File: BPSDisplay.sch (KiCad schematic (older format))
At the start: 22 parts, among them J1 SWD, J2 Conn_02x06_Counter_Clockwise, P1 Conn_02x20_Odd_Even, SW1 Reset, U1 STM32F413RHTx, Y1 8M

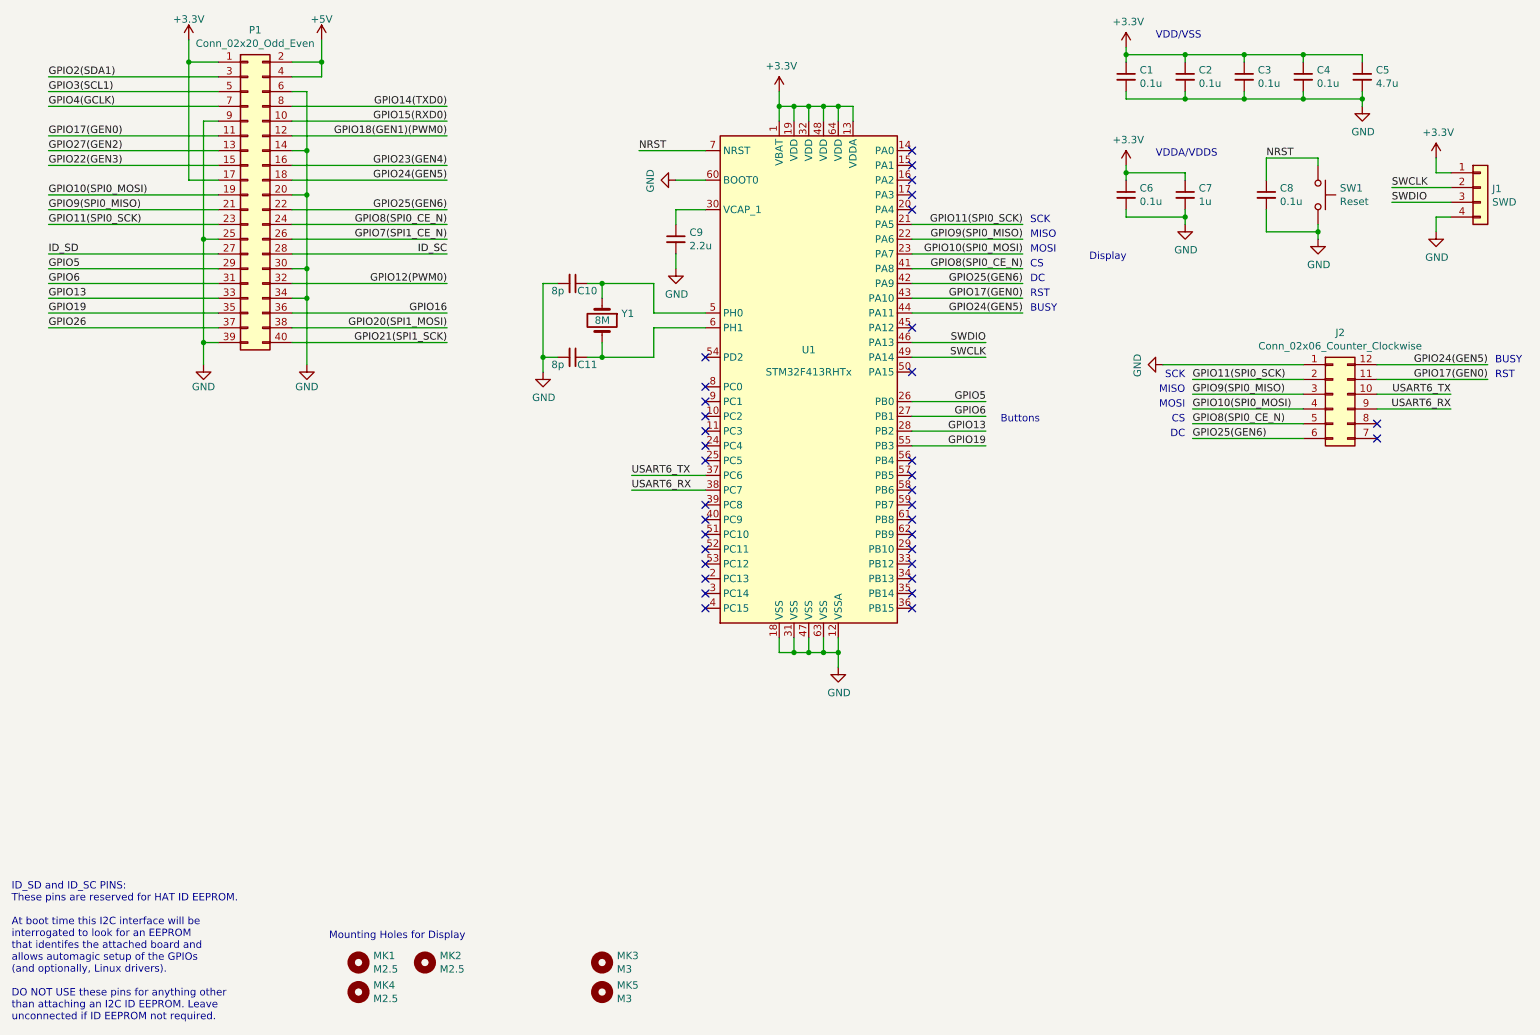
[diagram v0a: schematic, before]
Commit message: Deleted the isoSPI sheet and connections
On the schematic, I deleted the isoSPI sheet and its connections to the STM (replaced them with no connection flags). I updated the PCB from that so it now has all the components that need to be arranged and it can be done from scratch. I also added in a ground plane.
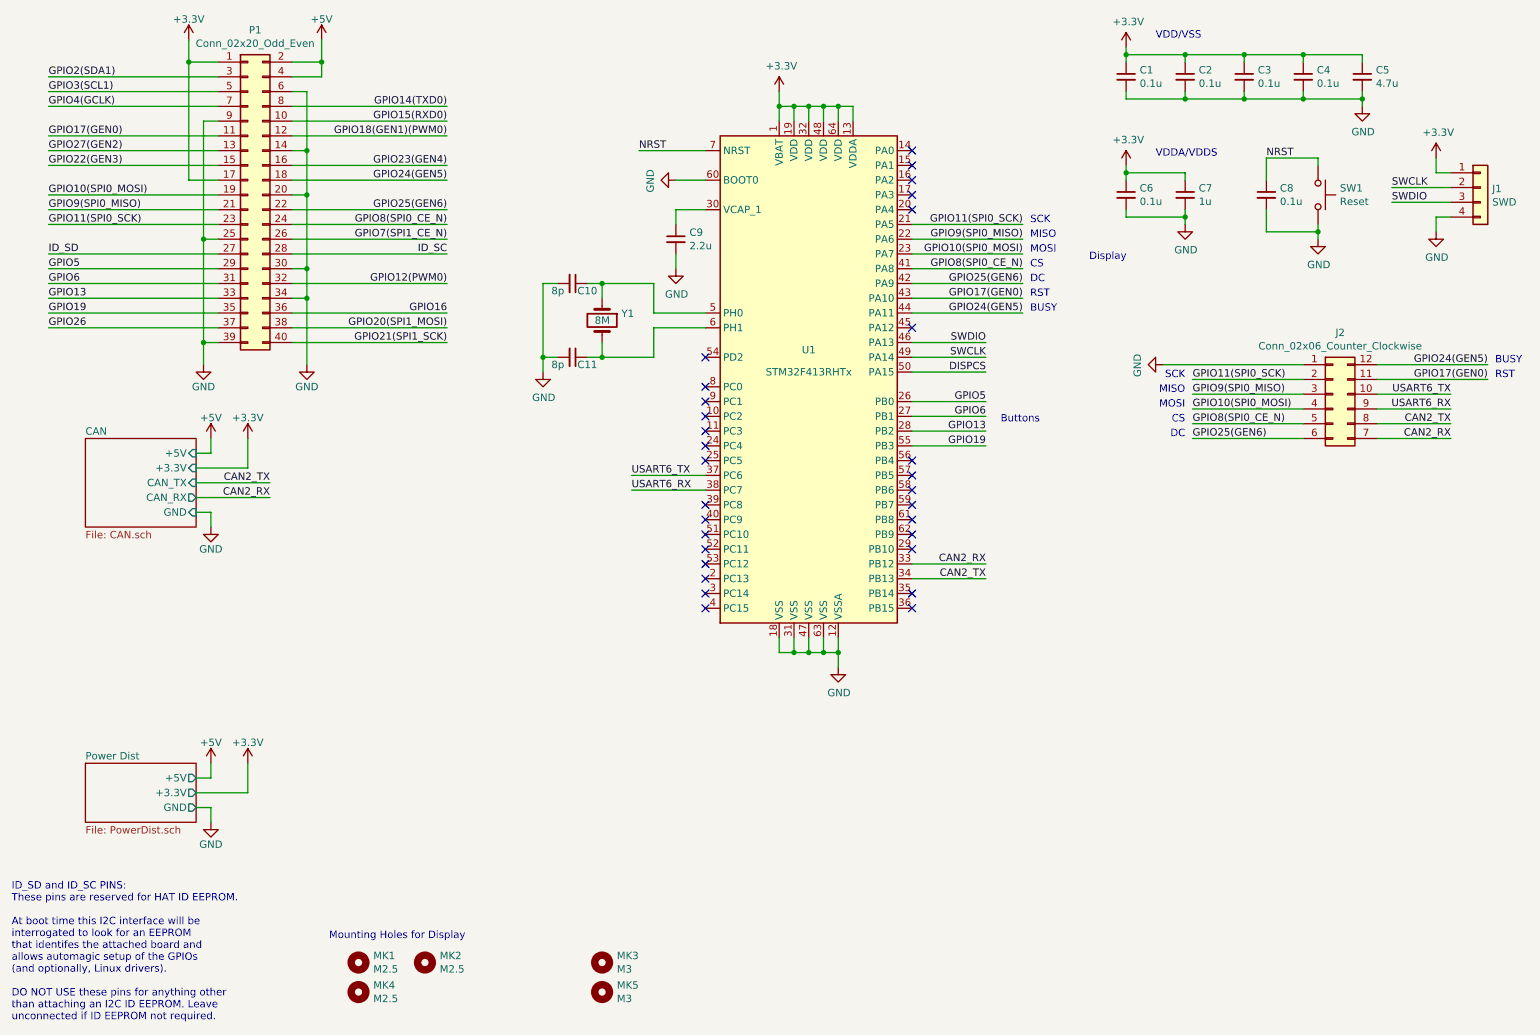
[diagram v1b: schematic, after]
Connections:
- net CAN2_RX: now reaches U1.33 (PB12)
- net CAN2_RX: now also J2.7 (Pin_7)
- net CAN2_TX: now reaches U1.34 (PB13)
- net CAN2_TX: now also J2.8 (Pin_8)
- net DISPCS: now reaches U1.50 (PA15)
- no-connect marks 35 -> 30
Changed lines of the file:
@@
 $Descr A4 11693 8268
 encoding utf-8
-Sheet 1 1
+Sheet 1 3
 Title ""
 Date "15 nov 2012"
@@
 Text Label 10000 1950 0    50   ~ 0
 SWCLK
+$Sheet
+S 1150 3650 750  600
+U 5D6B2C88
+F0 "CAN" 50
+F1 "CAN.sch" 50
+F2 "CAN_TX" I R 1900 3950 50
+F3 "CAN_RX" O R 1900 4050 50
+F4 "GND" I R 1900 4150 50
+F5 "+5V" I R 1900 3750 50
+F6 "+3.3V" I R 1900 3850 50
+$EndSheet
+$Comp
+L power:+5V #PWR017
+U 1 1 5D6BEA11
+P 2000 3650
+F 0 "#PWR017" H 2000 3500 50  0001 C CNN
+F 1 "+5V" H 2000 3790 50  0000 C CNN
+F 2 "" H 2000 3650 50  0000 C CNN
+F 3 "" H 2000 3650 50  0000 C CNN
+	1    2000 3650
+	1    0    0    -1
+$EndComp
+Wire Wire Line
+	1900 3750 2000 3750
+Wire Wire Line
+	2000 3750 2000 3650
+$Comp
+L power:+3.3V #PWR018
+U 1 1 5D6C6CA6
+P 2250 3650
+F 0 "#PWR018" H 2250 3500 50  0001 C CNN
+F 1 "+3.3V" H 2250 3790 50  0000 C CNN
+F 2 "" H 2250 3650 50  0000 C CNN
+F 3 "" H 2250 3650 50  0000 C CNN
+	1    2250 3650
+	1    0    0    -1
+$EndComp
+Wire Wire Line
+	2250 3650 2250 3850
+Wire Wire Line
+	6750 4500 7250 4500
+Wire Wire Line
+	7250 4600 6750 4600
+Text Label 7250 4600 2    50   ~ 0
+CAN2_TX
+Text Label 7250 4500 2    50   ~ 0
+CAN2_RX
+Wire Wire Line
+	1900 3950 2400 3950
+Wire Wire Line
+	2400 4050 1900 4050
+Text Label 2400 3950 2    50   ~ 0
+CAN2_TX
+Text Label 2400 4050 2    50   ~ 0
+CAN2_RX
+$Comp
+L power:GND #PWR019
+U 1 1 5D6E7067
+P 2000 4250
+F 0 "#PWR019" H 2000 4000 50  0001 C CNN
+F 1 "GND" H 2000 4100 50  0000 C CNN
+F 2 "" H 2000 4250 50  0000 C CNN
+F 3 "" H 2000 4250 50  0000 C CNN
+	1    2000 4250
+	1    0    0    -1
+$EndComp
+Wire Wire Line
+	2000 4250 2000 4150
+Wire Wire Line
+	2000 4150 1900 4150
+Wire Wire Line
+	2250 3850 1900 3850
+Wire Wire Line
+	6750 3200 7250 3200
+Text Label 7250 3200 2    50   ~ 0
+DISPCS
 $Comp
 L Connector_Generic:Conn_02x06_Counter_Clockwise J2
@@
 SCK
 Wire Wire Line
+	9900 3550 10400 3550
+Wire Wire Line
+	10400 3650 9900 3650
+Text Label 10400 3550 2    50   ~ 0
+CAN2_TX
+Text Label 10400 3650 2    50   ~ 0
+CAN2_RX
+Wire Wire Line
 	5350 3900 4850 3900
 Wire Wire Line
@@
 Text Label 10400 3450 2    50   ~ 0
 USART6_RX
+$Comp
+L power:GND #PWR025
+U 1 1 5D764CDB
+P 2000 6250
+F 0 "#PWR025" H 2000 6000 50  0001 C CNN
+F 1 "GND" H 2000 6100 50  0000 C CNN
+F 2 "" H 2000 6250 50  0000 C CNN
+F 3 "" H 2000 6250 50  0000 C CNN
+	1    2000 6250
+	1    0    0    -1
+$EndComp
+Wire Wire Line
+	2000 6250 2000 6150
+Wire Wire Line
+	2000 6150 1900 6150
+Wire Wire Line
+	1900 6050 2250 6050
+Wire Wire Line
+	2250 6050 2250 5850
+$Comp
+L power:+3.3V #PWR024
+U 1 1 5D771241
+P 2250 5850
+F 0 "#PWR024" H 2250 5700 50  0001 C CNN
+F 1 "+3.3V" H 2250 5990 50  0000 C CNN
+F 2 "" H 2250 5850 50  0000 C CNN
+F 3 "" H 2250 5850 50  0000 C CNN
+	1    2250 5850
+	1    0    0    -1
+$EndComp
+Wire Wire Line
+	2000 5950 2000 5850
+$Comp
+L power:+5V #PWR023
+U 1 1 5D77123B
+P 2000 5850
+F 0 "#PWR023" H 2000 5700 50  0001 C CNN
+F 1 "+5V" H 2000 5990 50  0000 C CNN
+F 2 "" H 2000 5850 50  0000 C CNN
+F 3 "" H 2000 5850 50  0000 C CNN
+	1    2000 5850
+	1    0    0    -1
+$EndComp
+Wire Wire Line
+	1900 5950 2000 5950
+$Sheet
+S 1150 5850 750  400
+U 5D76E7C8
+F0 "Power Dist" 50
+F1 "PowerDist.sch" 50
+F2 "GND" O R 1900 6150 50
+F3 "+3.3V" O R 1900 6050 50
+F4 "+5V" O R 1900 5950 50
+$EndSheet
 $Comp
 L power:GND #PWR08
@@
 Wire Wire Line
 	9800 1400 9800 1350
-NoConn ~ 6750 4500
-NoConn ~ 6750 4600
 NoConn ~ 5350 4300
 NoConn ~ 5350 4400
 NoConn ~ 5350 4500
-NoConn ~ 6750 3200
-NoConn ~ 9900 3550
-NoConn ~ 9900 3650
 $EndSCHEMATC
